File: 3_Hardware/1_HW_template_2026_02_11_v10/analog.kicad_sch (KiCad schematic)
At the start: 8 parts, among them U3 MCP6002-xSN, Y2 ${SIM.PARAMS}

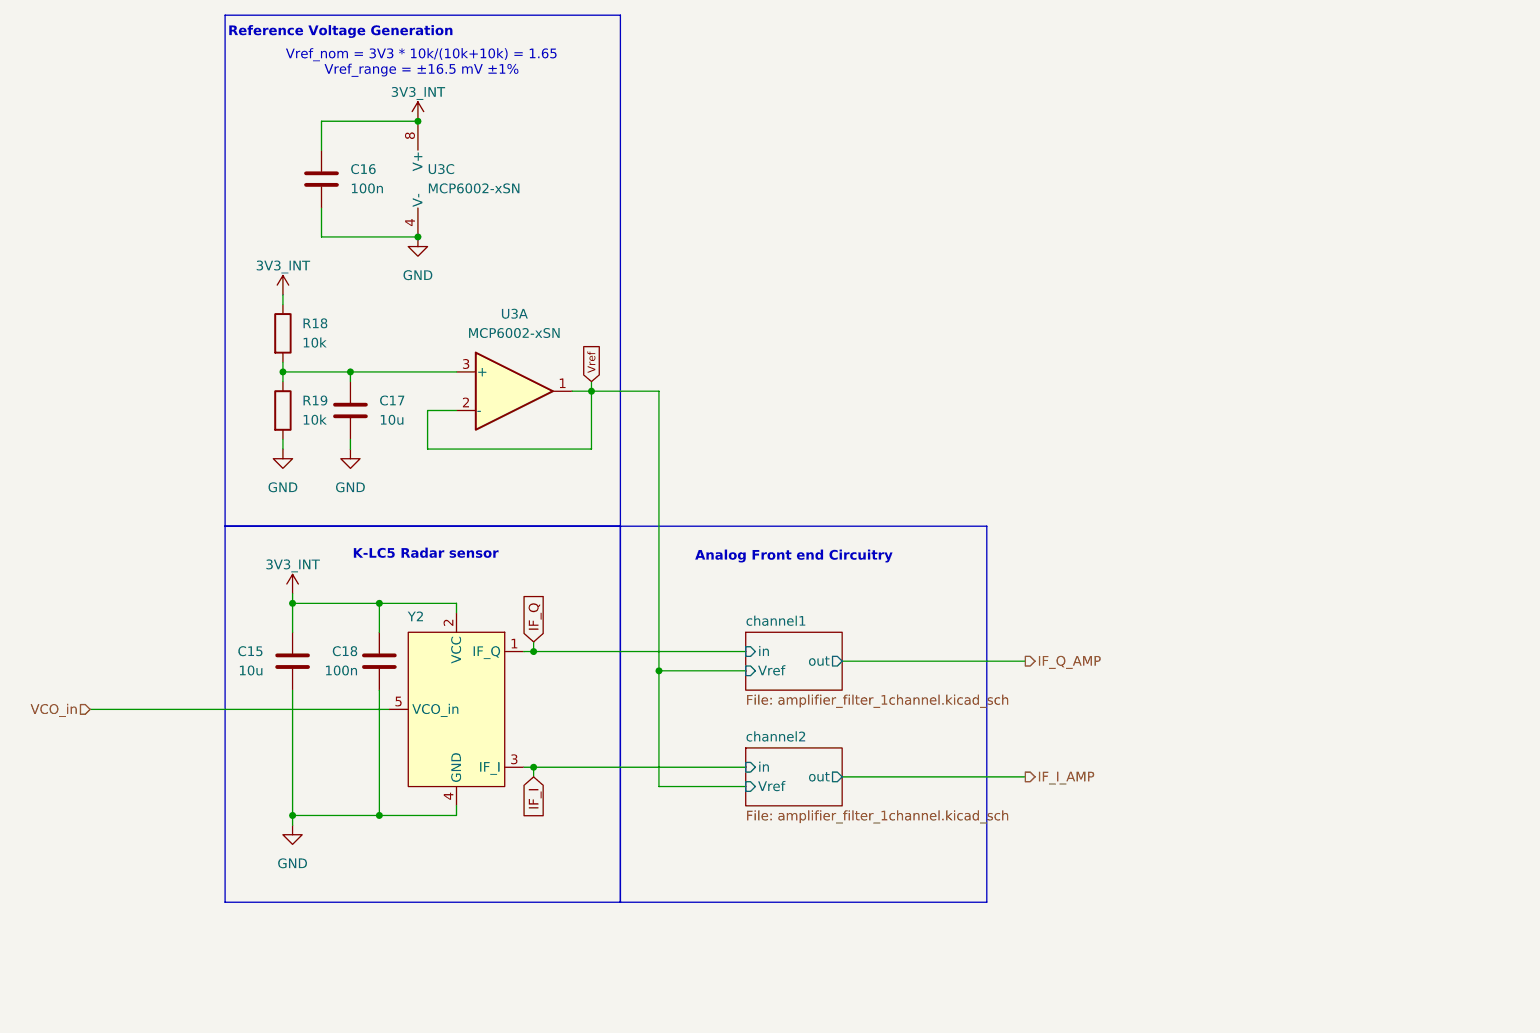
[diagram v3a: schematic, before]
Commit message: added AD8232
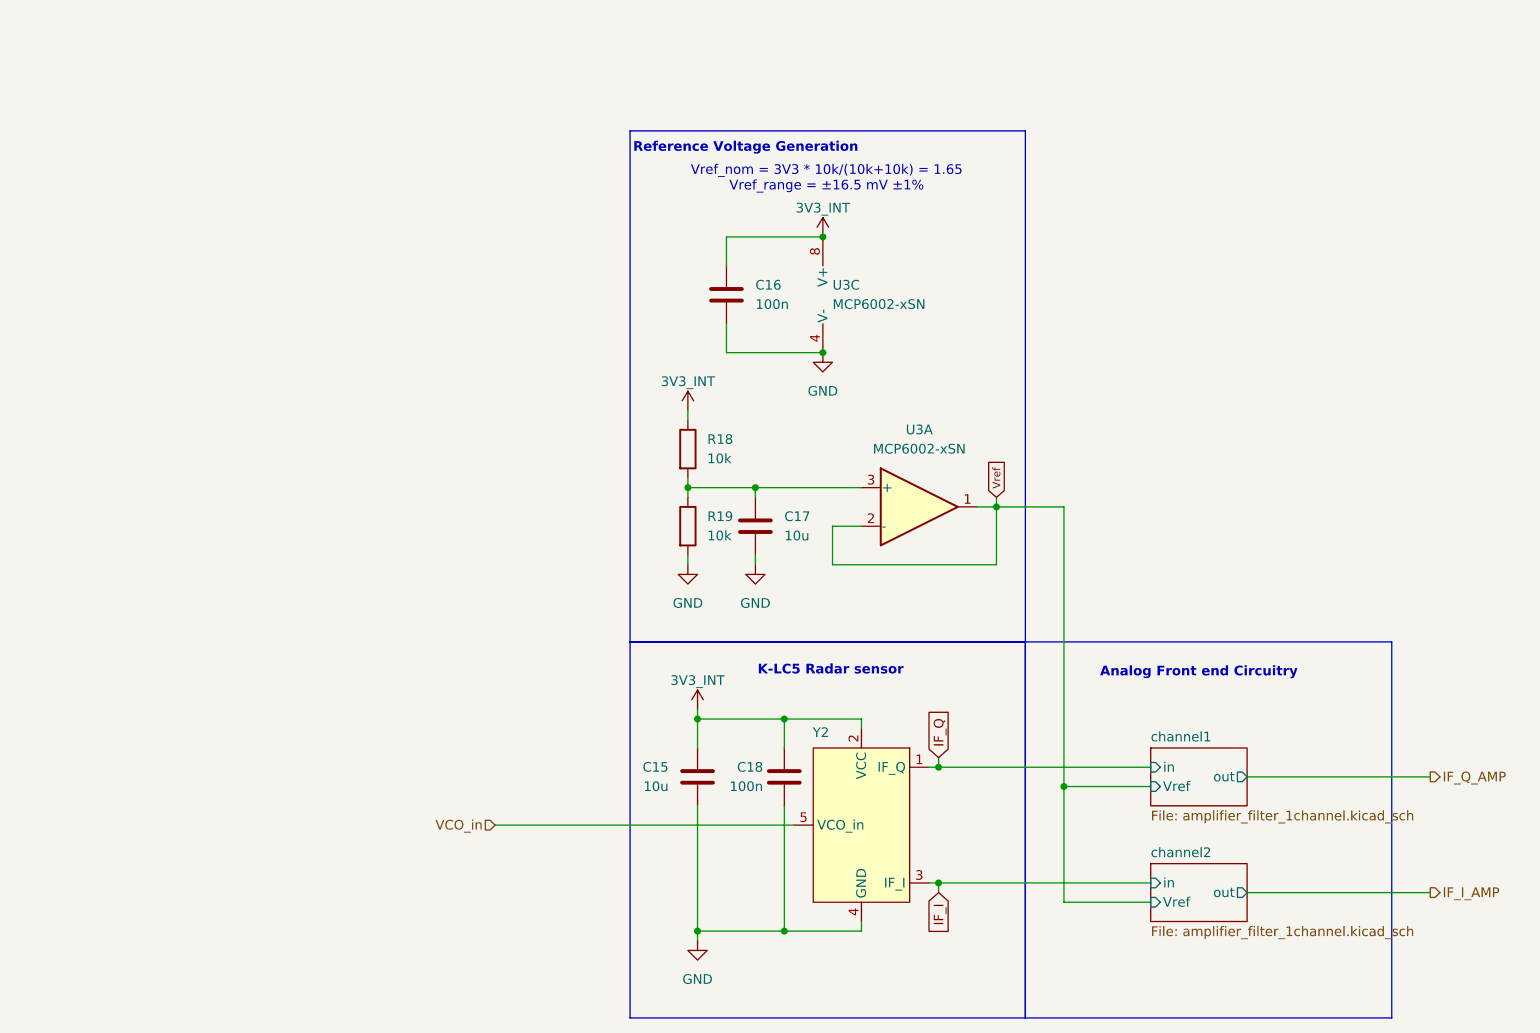
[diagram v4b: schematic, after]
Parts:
- C15, C18: footprint Capacitor_SMD:C_0805_2012Metric_Pad1.18x1.45mm_HandSolder -> Capacitor_SMD:C_0603_1608Metric_Pad1.08x0.95mm_HandSolder
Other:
- moved on the sheet: C15, C16, C17, C18, R18, R19, U3A, U3C, Y2

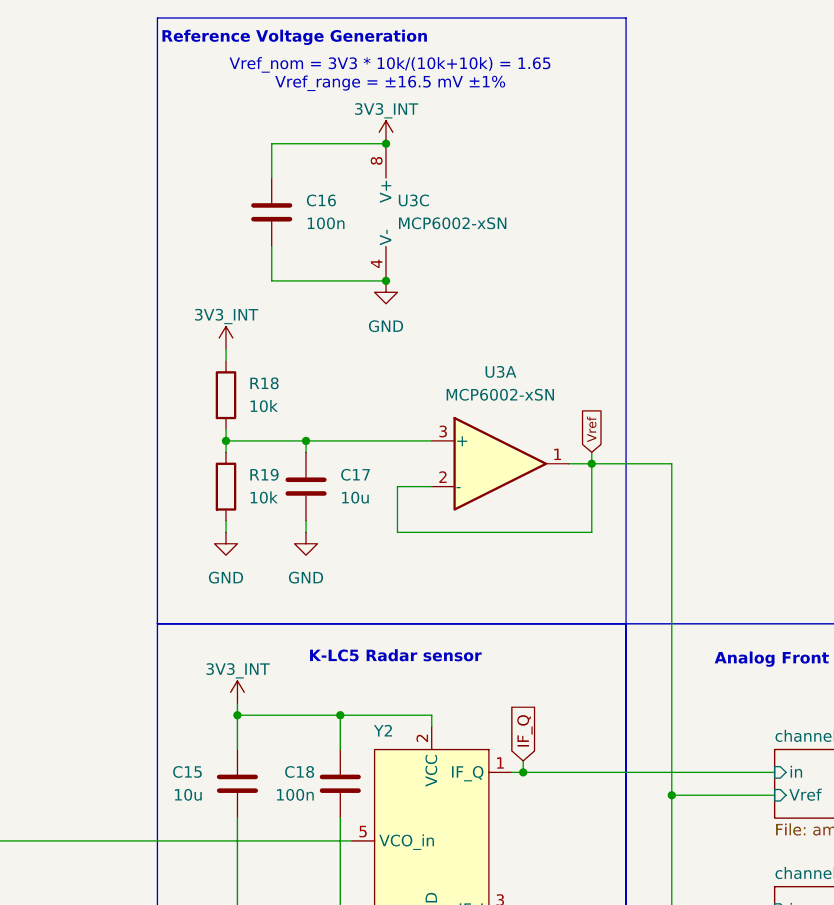
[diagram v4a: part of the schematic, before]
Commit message: updated layout
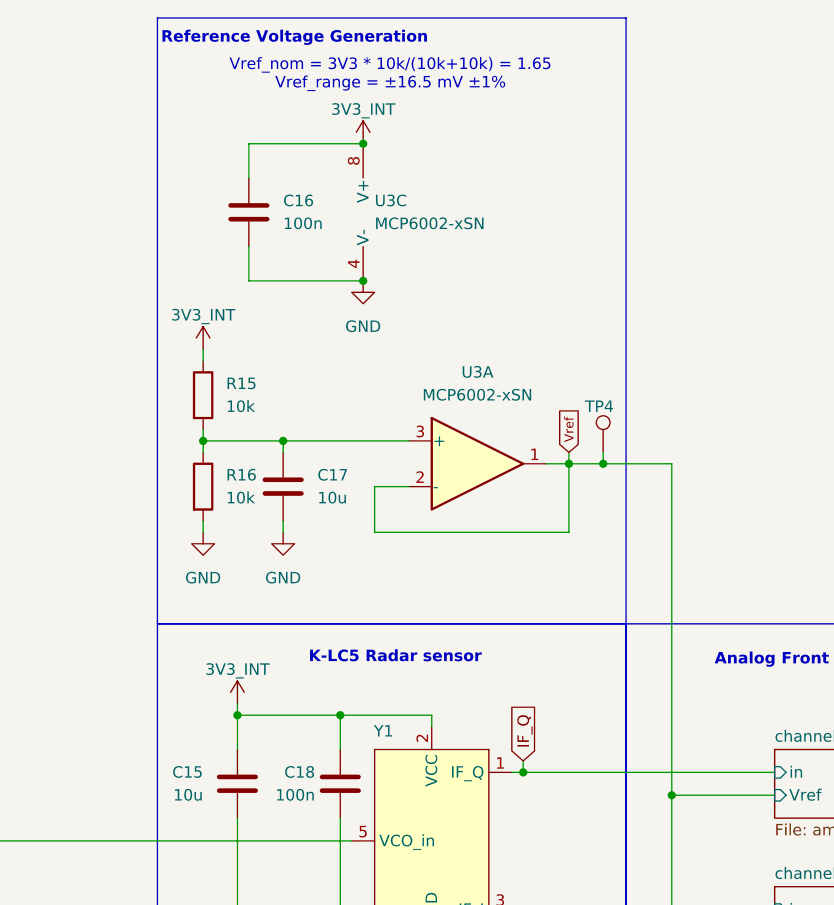
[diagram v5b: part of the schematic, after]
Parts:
- added TP4: Channel1, TestPoint:TestPoint_Loop_D2.60mm_Drill1.6mm_Beaded, symbol Connector:TestPoint
- renumbered R18 to R15, R19 to R16, Y2 to Y1
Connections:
- net Vref: now also TP4.1
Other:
- moved on the sheet: C16, C17, R15, R16, U3A, U3C

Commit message: fixed footprints
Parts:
- C16, C17: footprint Capacitor_SMD:C_0805_2012Metric_Pad1.18x1.45mm_HandSolder -> Capacitor_SMD:C_0603_1608Metric_Pad1.08x0.95mm_HandSolder
- R15, R16: footprint Resistor_SMD:R_0805_2012Metric_Pad1.20x1.40mm_HandSolder -> Resistor_SMD:R_0603_1608Metric_Pad0.98x0.95mm_HandSolder
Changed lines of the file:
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@@
 			)
 		)
-		(property "Footprint" "Resistor_SMD:R_0805_2012Metric_Pad1.20x1.40mm_HandSolder"
+		(property "Footprint" "Resistor_SMD:R_0603_1608Metric_Pad0.98x0.95mm_HandSolder"
 			(at 103.632 86.36 90)
 			(effects
@@
 			)
 		)
-		(property "Footprint" "Capacitor_SMD:C_0805_2012Metric_Pad1.18x1.45mm_HandSolder"
+		(property "Footprint" "Capacitor_SMD:C_0603_1608Metric_Pad1.08x0.95mm_HandSolder"
 			(at 111.4552 59.69 0)
 			(effects
@@
 			)
 		)
-		(property "Footprint" "Capacitor_SMD:C_0805_2012Metric_Pad1.18x1.45mm_HandSolder"
+		(property "Footprint" "Capacitor_SMD:C_0603_1608Metric_Pad1.08x0.95mm_HandSolder"
 			(at 115.2652 90.17 0)
 			(effects
@@
 			)
 		)
-		(property "Footprint" "Resistor_SMD:R_0805_2012Metric_Pad1.20x1.40mm_HandSolder"
+		(property "Footprint" "Resistor_SMD:R_0603_1608Metric_Pad0.98x0.95mm_HandSolder"
 			(at 103.632 76.2 90)
 			(effects

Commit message: minor pcb improvements + bom
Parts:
- TP4: value Channel1 -> ~
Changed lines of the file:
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@@
 			)
 		)
-		(property "Value" "Channel1"
+		(property "Value" "~"
 			(at 152.4 80.5179 0)
 			(effects
